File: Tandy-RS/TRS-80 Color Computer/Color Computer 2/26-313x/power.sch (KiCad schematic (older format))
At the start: 24 parts, among them IC1 SC77527, Q1 2SD313 (E), SW1 SW_DPST, T1 TRANSF4

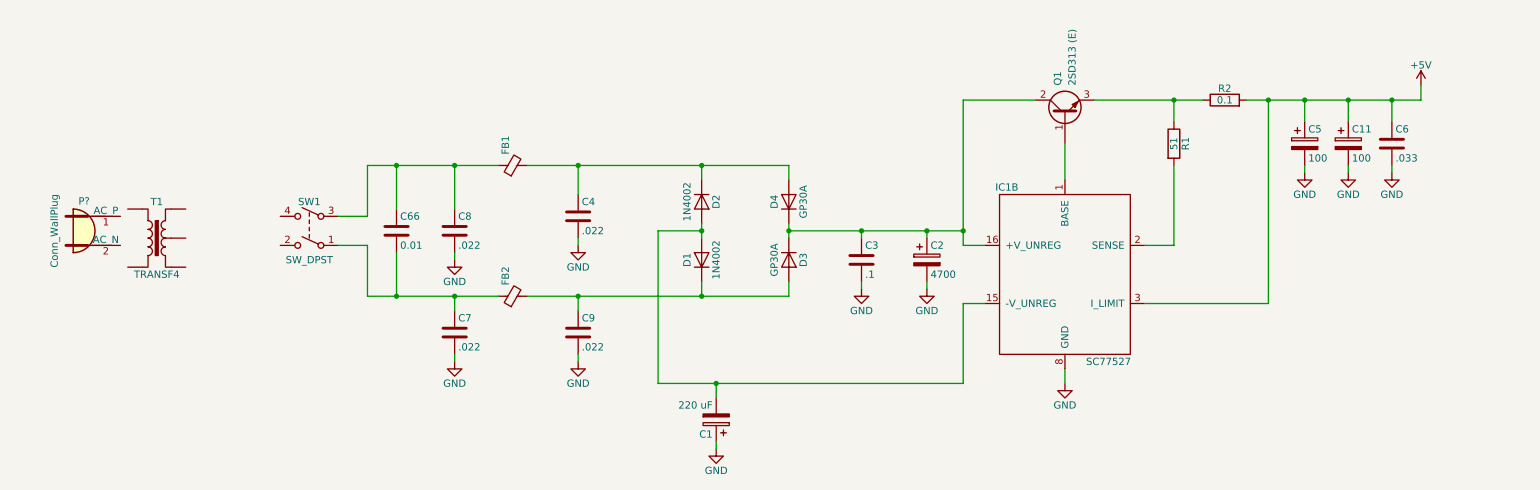
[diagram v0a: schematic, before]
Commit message: Complete video schematic
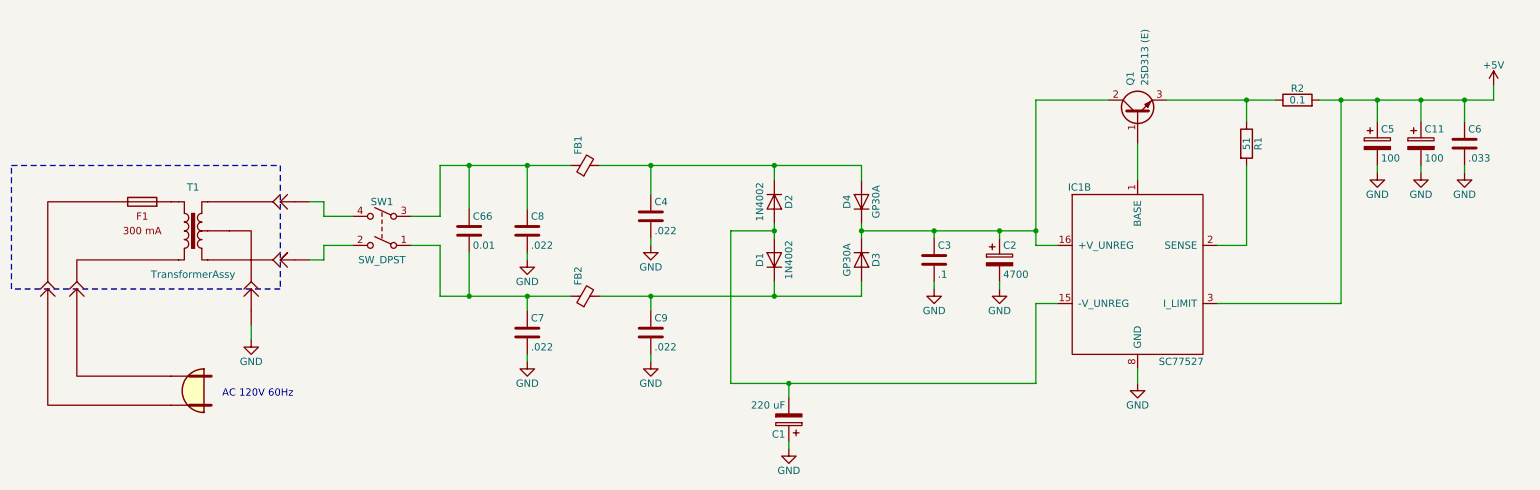
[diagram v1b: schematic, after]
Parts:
- removed P?: Conn_WallPlug, symbol Connector:Conn_WallPlug
- removed T1: TRANSF4, symbol Transformer:TRANSF4
- added T1: TransformerAssy, symbol coco2:TransformerAssy
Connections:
- net GND: now also T1.2
- net at SW1.2: now also T1.3
- net at SW1.4: now also T1.1
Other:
- note added: "AC 120V 60Hz"
- moved on the sheet: C1, C11, C2, C3, C4, C5, C6, C66, C7, C8, C9, D1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

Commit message: Finish drawing initial version of Coco2 schematic
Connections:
- wire segments 81 -> 84
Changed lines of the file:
@@
 $Descr A4 11693 8268
 encoding utf-8
-Sheet 2 5
-Title ""
-Date ""
-Rev ""
-Comp ""
-Comment1 ""
+Sheet 2 8
+Title "TRS-80 Color Computer 2 (26-3134 / 26-3136) - Power"
+Date "2020-10-14"
+Rev "0.1"
+Comp "Tandy Corporation"
+Comment1 "Based on \"Service Manual TRS-80 Color Computer 2 NTSC Version\" pp. 87"
 Comment2 ""
 Comment3 ""
-Comment4 ""
+Comment4 "Kicad schematic capture by troysbucket"
 $EndDescr
 $Comp
@@
 Connection ~ 3900 3650
 Wire Wire Line
-	3900 3650 4300 3650
-Wire Wire Line
 	4300 3950 4300 3650
 Connection ~ 4300 3650
@@
 Wire Wire Line
 	3700 4550 3900 4550
-Wire Wire Line
-	3900 4550 4300 4550
 Wire Wire Line
 	4300 4650 4300 4550
@@
 	6000 3750 6000 3650
 Wire Wire Line
-	6000 3650 6600 3650
-Wire Wire Line
 	6600 3650 6600 3750
 Wire Wire Line
@@
 Connection ~ 6000 3650
 Wire Wire Line
-	6000 4550 6600 4550
-Wire Wire Line
 	4800 4550 5150 4550
 Connection ~ 6000 4550
@@
 Wire Wire Line
 	5150 4550 6000 4550
-$Comp
-L Device:CP C1
-U 1 1 5F446734
-P 6100 5400
-F 0 "C1" H 6125 5500 50  0000 L CNN
-F 1 "220 uF" H 6125 5300 50  0000 L CNN
-F 2 "" H 6138 5250 50  0001 C CNN
-F 3 "~" H 6100 5400 50  0001 C CNN
-F 4 "16V" H 6100 5400 50  0001 C CNN "Voltage"
-F 5 "20%" H 6100 5400 50  0001 C CNN "Tolerance"
-	1    6100 5400
-	-1   0    0    1
-$EndComp
 Wire Wire Line
 	6000 4100 5700 4100
@@
 	1    0    0    -1
 $EndComp
-Wire Wire Line
-	6100 5550 6100 5600
-Wire Wire Line
-	6100 5250 6100 5150
-Wire Wire Line
-	5700 5150 6100 5150
 $Comp
 L Device:C C3
@@
 Connection ~ 10450 3200
 Wire Wire Line
-	10450 3200 10750 3200
+	10450 3200 10600 3200
 Wire Wire Line
 	10150 3350 10150 3200
@@
 Connection ~ 10750 3200
 Wire Wire Line
-	6100 5150 7800 5150
-Wire Wire Line
 	7800 5150 7800 4600
 Wire Wire Line
 	7800 4600 7950 4600
-Connection ~ 6100 5150
 Wire Wire Line
 	6600 4100 7100 4100
@@
 Connection ~ 7100 4100
 Wire Wire Line
-	7100 4100 7550 4100
+	7100 4100 7400 4100
 $Comp
 L coco2:TransformerAssy T1
@@
 AC 120V 60Hz
 Wire Wire Line
-	2800 3900 2900 3900
-Wire Wire Line
 	2900 3900 2900 4000
 Wire Wire Line
 	2900 4000 3100 4000
-Wire Wire Line
-	2800 4300 2900 4300
 Wire Wire Line
 	2900 4300 2900 4200
@@
 Wire Wire Line
 	2400 4750 2400 4850
+$Comp
+L Device:CP C1
+U 1 1 5F446734
+P 6100 5400
+F 0 "C1" H 5900 5300 50  0000 L CNN
+F 1 "220 uF" H 5750 5550 50  0000 L CNN
+F 2 "" H 6138 5250 50  0001 C CNN
+F 3 "~" H 6100 5400 50  0001 C CNN
+F 4 "16V" H 6100 5400 50  0001 C CNN "Voltage"
+F 5 "20%" H 6100 5400 50  0001 C CNN "Tolerance"
+	1    6100 5400
+	-1   0    0    1
+$EndComp
+Wire Wire Line
+	6100 5550 6100 5600
+Wire Wire Line
+	6100 5150 7400 5150
+Wire Wire Line
+	5700 5150 6100 5150
+Connection ~ 6100 5150
+Wire Wire Line
+	6100 5250 6100 5150
+$Comp
+L power:PWR_FLAG #FLG0107
+U 1 1 5F8FE177
+P 7400 4100
+F 0 "#FLG0107" H 7400 4175 50  0001 C CNN
+F 1 "PWR_FLAG" H 7400 4250 50  0000 C CNN
+F 2 "" H 7400 4100 50  0001 C CNN
+F 3 "~" H 7400 4100 50  0001 C CNN
+	1    7400 4100
+	1    0    0    -1
+$EndComp
+Connection ~ 7400 4100
+Wire Wire Line
+	7400 4100 7550 4100
+Wire Wire Line
+	6000 3650 6600 3650
+Wire Wire Line
+	6000 4550 6600 4550
+Wire Wire Line
+	3900 4550 4300 4550
+Wire Wire Line
+	3900 3650 4300 3650
+Wire Wire Line
+	2800 3900 2900 3900
+Wire Wire Line
+	2800 4300 2900 4300
+$Comp
+L power:PWR_FLAG #FLG0101
+U 1 1 5F8FF1DD
+P 7400 5150
+F 0 "#FLG0101" H 7400 5225 50  0001 C CNN
+F 1 "PWR_FLAG" H 7400 5300 50  0000 C CNN
+F 2 "" H 7400 5150 50  0001 C CNN
+F 3 "~" H 7400 5150 50  0001 C CNN
+	1    7400 5150
+	1    0    0    -1
+$EndComp
+Connection ~ 7400 5150
+Wire Wire Line
+	7400 5150 7800 5150
+$Comp
+L power:PWR_FLAG #FLG0103
+U 1 1 5F927B03
+P 10600 3200
+F 0 "#FLG0103" H 10600 3275 50  0001 C CNN
+F 1 "PWR_FLAG" H 10600 3350 50  0000 C CNN
+F 2 "" H 10600 3200 50  0001 C CNN
+F 3 "~" H 10600 3200 50  0001 C CNN
+	1    10600 3200
+	1    0    0    -1
+$EndComp
+Connection ~ 10600 3200
+Wire Wire Line
+	10600 3200 10750 3200
 $EndSCHEMATC
